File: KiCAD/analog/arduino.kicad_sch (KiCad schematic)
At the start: 49 parts, among them J12 Screw_Terminal_01x04, J13 Screw_Terminal_01x03, J14 Screw_Terminal_01x05, J17 Conn_Coaxial_Small, J18 Conn_Coaxial_Small, J19 Conn_Coaxial_Small, J20 Screw_Terminal_01x04, J21 Screw_Terminal_01x02, J22 Screw_Terminal_01x04, J23 Conn_Coaxial_Small, J24 Conn_Coaxial_Small, J6 Screw_Terminal_01x02, J7 Screw_Terminal_01x02, J8 Screw_Terminal_01x02, J9 Screw_Terminal_01x02, Q4 2N7000, Q5 2N7000, Q6 2N7000, Q7 2N7000, U1 MCP1700x-330xxTO, U17 Adafruit_PCF8575_Breakout, U18 CD14538B, U3 MCP4728

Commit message: KiCad revB: custom footprints, coax assignments, TO-92 widening, ENC_INT rewire
Second-pass footprint work: filled the remaining empty footprints
that couldn't be handled by the earlier stock-library scripts, added
custom footprints for parts KiCad's stock library doesn't cover, and
did a few schematic hygiene fixes surfaced during the deep-dive
reviews.

Custom footprints (new, xmitter.pretty/):
- SMA_Cinch_142-0701-201_Vertical_JackPCB - 50 Ohm SMA vertical
  through-hole jack for the analog board and bias board coax
  interconnects (I_CATHODE, GRID_CTL, GRID_BLOCK_CRASH, GRID_BIAS).
  Center pin 1.57 mm hole + 4 ground tabs on a 5.08 mm square
  pattern. All 4 ground tabs share pin number 2 (shield).
- CP_Radial_Kemet_ESK_D22.0mm_P10.00mm - Kemet ESK case Q4 radial
  electrolytic (22 mm dia, 10 mm pitch) for C72 = 4700 uF 50V.
- Fuse_Littelfuse_60R_L7.9mm_W3.1mm_P5.08mm - Littelfuse 60R Series
  radial polyfuse for F1 = 60R050XU (0.5 A hold). Body sized for the
  small-body variants (010X-090X); pitch 5.08 mm, drill 0.7 mm.
- C_Axial_Kemet_Aximax_C41X_L4.5mm_D2.6mm_P7.62mm_Horizontal - Kemet
  Aximax C410 axial C0G ceramic for the three 2 pF caps
  (C69/C70/C71) in the vfo_complete keyer chain. Horizontal mount,
  7.62 mm pitch.

New re-runnable script:
- tools/assign_coax_footprints.py - maps
  Connector:Conn_Coaxial_Small symbols to the new Cinch SMA
  footprint. Same "only fill empty, never overwrite" pattern as the
  existing assign_*_footprints.py scripts.

Script extension:
- tools/assign_cap_footprints.py - added value entries for 4700uF
  (Kemet ESK), 220nF (D6 disc), 2pF (Kemet Aximax C41X), and 100uF
  (Vishay 036 RSP). All four entries include the datasheet path and
  the specific case-size rationale.

Schematic edits (all boards):
- 12 coax connectors assigned to the new Cinch SMA footprint
  (analog J17-J19/J23-J24, bias J1/J2/J4/J6/J9/J10/J12) via the new
  assign_coax script.
- 5 caps in vfo_complete assigned via extended assign_cap_footprints
  (C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
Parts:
- F1: footprint (none) -> xmitter:Fuse_Littelfuse_60R_L7.9mm_W3.1mm_P5.08mm
- J17, J18, J19, J23, J24: footprint (none) -> xmitter:SMA_Cinch_142-0701-201_Vertical_JackPCB
- U1: footprint Package_TO_SOT_THT:TO-92_Inline -> Package_TO_SOT_THT:TO-92_Inline_Wide
- U3: footprint (none) -> xmitter:Adafruit_MCP4728_Breakout
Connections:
- net ENC_INT: now also C7.1, J9.2 (Pin_2), R6.2, R7.2; no longer R6.1
- net ENC_INT_CLEAN: now also R6.1; no longer C7.1, J9.2 (Pin_2), R6.2, R7.2
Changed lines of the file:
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@@
 		)
 	)
-	(global_label "ENC_INT_CLEAN"
+	(global_label "ENC_INT"
 		(shape input)
 		(at 46.99 66.04 90)
@@
 		)
 	)
-	(global_label "ENC_INT"
+	(global_label "ENC_INT_CLEAN"
 		(shape input)
 		(at 73.66 66.04 0)
@@
 			)
 		)
-		(property "Footprint" ""
+		(property "Footprint" "xmitter:Adafruit_MCP4728_Breakout"
 			(at 69.85 35.56 0)
 			(hide yes)
@@
 			)
 		)
-		(property "Footprint" ""
+		(property "Footprint" "xmitter:SMA_Cinch_142-0701-201_Vertical_JackPCB"
 			(at 121.92 119.38 0)
 			(hide yes)
@@
 			)
 		)
-		(property "Footprint" ""
+		(property "Footprint" "xmitter:SMA_Cinch_142-0701-201_Vertical_JackPCB"
 			(at 95.25 40.64 0)
 			(hide yes)
@@
 			)
 		)
-		(property "Footprint" ""
+		(property "Footprint" "xmitter:SMA_Cinch_142-0701-201_Vertical_JackPCB"
 			(at 78.74 157.48 0)
 			(hide yes)
@@
 			)
 		)
-		(property "Footprint" ""
+		(property "Footprint" "xmitter:SMA_Cinch_142-0701-201_Vertical_JackPCB"
 			(at 95.25 36.83 0)
 			(hide yes)
@@
 			)
 		)
-		(property "Footprint" ""
+		(property "Footprint" "xmitter:SMA_Cinch_142-0701-201_Vertical_JackPCB"
 			(at 118.11 138.43 0)
 			(hide yes)
@@
 			)
 		)
-		(property "Footprint" ""
+		(property "Footprint" "xmitter:Fuse_Littelfuse_60R_L7.9mm_W3.1mm_P5.08mm"
 			(at 104.14 99.06 0)
 			(hide yes)
@@
 			)
 		)
-		(property "Footprint" "Package_TO_SOT_THT:TO-92_Inline"
+		(property "Footprint" "Package_TO_SOT_THT:TO-92_Inline_Wide"
 			(at 173.99 25.4 0)
 			(hide yes)

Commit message: revB frozen state: MCP4922 swap + LDAC decouple + sheet rename + protoshield work
Captures the in-flight state of revB at the point where the project pivoted
to a full-SS output stage on a new branch (SS_Rev_C, cut from this commit).
revB is retained as a fallback if the SS PA plan on revC proves inadequate.

Included changes:
- Analog: MCP4921 (single DAC) replaced with MCP4922 (dual DAC). Channel
  assignment: DAC_A -> PA_OUTPUT_LEVEL (new global label, awaiting PA
  board), DAC_B -> Gate 2 (DGFET envelope keyer). Channels swapped from
  initial-design intent for layout convenience.
- Analog: DAC_LDAC_N decoupled from PCF8575 P5 (that global label renamed
  to PCF_P5_SPARE). Intent: route LDAC to Metro A4 for zero-latency
  simultaneous-DAC-update capability. Physical route to A4 NOT yet added
  -- DAC_LDAC_N label on dac.kicad_sch is dangling and will fail ERC.
- Analog: KiCad-driven used_designators bookkeeping (analog.kicad_pro).
- Sheet rename: KiCAD/analog/untitled.kicad_sch -> dac.kicad_sch. Root
  schematic Sheetfile reference updated.
- Protoshield: 537 lines of additions to protoshield.kicad_sch (user
  work). Not reviewed in this commit -- carried forward as-is.
- .gitignore: added tools/_*.py exclusion (local review-helper scripts).

**revB is NOT fab-ready in this state.** See memory
project_revB_pre_fab_check.md (outside repo) for the punch list. If the
SS PA plan ever reverses and someone revives revB, ALL open items must
be closed and a full pass through Documentation/pcb_fab_checklist.md
must be completed before any gerber submit.

Co-Authored-By: Claude Opus 4.7 <noreply@anthropic.com>
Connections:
- net GND: no longer J14.4 (Pin_4)
- net DAC_SHDN_N: now reaches U17.P6
- new net PCF_P5_SPARE: J14.4 (Pin_4)
- no-connect marks 23 -> 22
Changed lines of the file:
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@@
 	)
 	(no_connect
-		(at 175.26 81.28)
-	)
-	(no_connect
 		(at 175.26 68.58)
 	)
@@
 	)
 	(no_connect
-		(at 175.26 83.82)
+		(at 175.26 81.28)
 	)
 	(no_connect
@@
 		)
 	)
+	(global_label "PCF_P5_SPARE"
+		(shape input)
+		(at 30.48 110.49 0)
+		(fields_autoplaced yes)
+		(effects
+			(font
+				(size 1.27 1.27)
+			)
+			(justify left)
+		)
+		(property "Intersheetrefs" "${INTERSHEET_REFS}"
+			(at 45.0162 110.49 0)
+			(hide yes)
+			(show_name no)
+			(do_not_autoplace no)
+			(effects
+				(font
+					(size 1.27 1.27)
+				)
+				(justify left)
+			)
+		)
+	)
 	(global_label "GRID_CTL_B"
 		(shape output)
@@
 		)
 	)
+	(global_label "DAC_SHDN_N"
+		(shape output)
+		(at 175.26 83.82 180)
+		(fields_autoplaced yes)
+		(effects
+			(font
+				(size 1.27 1.27)
+			)
+			(justify right)
+		)
+		(property "Intersheetrefs" "${INTERSHEET_REFS}"
+			(at 160.24 83.82 0)
+			(hide yes)
+			(show_name no)
+			(do_not_autoplace no)
+			(effects
+				(font
+					(size 1.27 1.27)
+				)
+				(justify right)
+			)
+		)
+	)
 	(global_label "GRID_BLOCK_CRASH"
 		(shape input)
@@
 					(unit 1)
 				)
-			)
-		)
-	)
-	(symbol
-		(lib_id "power:GND")
-		(at 30.48 110.49 90)
-		(unit 1)
-		(body_style 1)
-		(exclude_from_sim no)
-		(in_bom yes)
-		(on_board yes)
-		(in_pos_files yes)
-		(dnp no)
-		(fields_autoplaced yes)
-		(property "Reference" "#PWR010"
-			(at 36.83 110.49 0)
-			(hide yes)
-			(show_name no)
-			(do_not_autoplace no)
-			(effects
-				(font
-					(size 1.27 1.27)
-				)
-			)
-		)
-		(property "Value" "GND"
-			(at 34.29 110.4899 90)
-			(show_name no)
-			(do_not_autoplace no)
-			(effects
-				(font
-					(size 1.27 1.27)
-				)
-				(justify right)
-			)
-		)
-		(property "Footprint" ""
-			(at 30.48 110.49 0)
-			(hide yes)
-			(show_name no)
-			(do_not_autoplace no)
-			(effects
-				(font
-					(size 1.27 1.27)
-				)
-			)
-		)
-		(property "Datasheet" ""
-			(at 30.48 110.49 0)
-			(hide yes)
-			(show_name no)
-			(do_not_autoplace no)
-			(effects
-				(font
-					(size 1.27 1.27)
-				)
-			)
-		)
-		(property "Description" "Power symbol creates a global label with name \"GND\" , ground"
-			(at 30.48 110.49 0)
-			(hide yes)
-			(show_name no)
-			(do_not_autoplace no)
-			(effects
-				(font
-					(size 1.27 1.27)
-				)
-			)
-		)
-		(pin "1"
-		)
-		(instances
-			(project "analog"
-				(path "/d3de40b8-856b-4fbd-829c-f45ffcd55742/2d83d0b5-86d4-4ced-ab68-6465e3dc2d72"
-					(reference "#PWR010")
-					(unit 1)
-				)

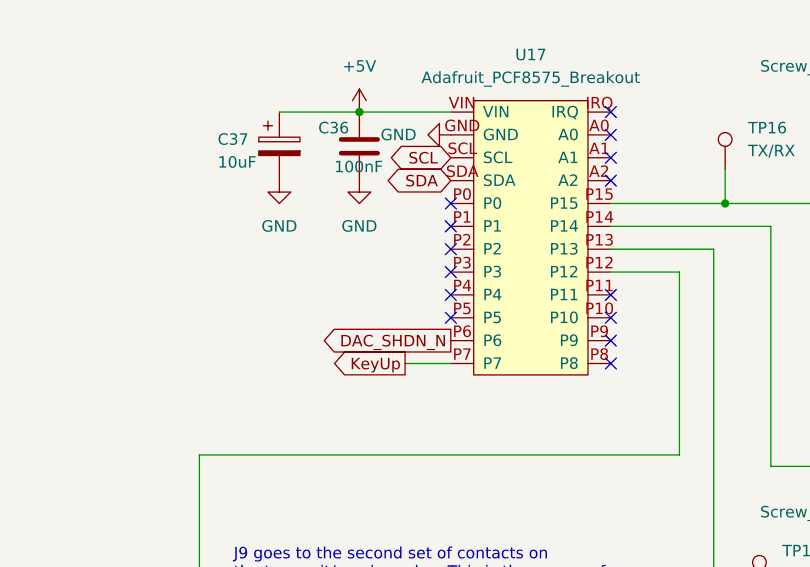
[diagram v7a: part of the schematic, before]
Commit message: KiCad revC: 4-band LPF bank populated + pad values + A_L units fix
Analog board revC: the LPF sheet is now fully populated with the
4-band relay-switched LPF bank architecture discussed in prior
sessions.  VFO sheet refactored to remove the old single-LPF stage.

LPF bank (lpf.kicad_sch):
  - 4 branches tied to a common input bus from U2 (LM7171 buffer).
    Common bus driven through C9 100nF; U2 non-inverting gain = 5.7.
  - Per-branch: 10 dB pi attenuator (100/68/100 ohm) -> 7-element
    Chebyshev CLCLCLC LPF (0.1 dB ripple, 50 ohm) -> 50 ohm RT
    terminator -> SPST relay (K1-K4) -> common output bus
    "Conditioned RF" -> R39 (0R) -> U10 input on VFO sheet.
  - Relay drive: 2N7000 low-side switcher (Q1/Q3/Q8/Q9) + 1N4148
    flyback diode (D7-D10) + screw terminal (J16/J25/J26/J27) per
    relay for coil wire termination.
  - LPF components: CF3-CF21 and L4-L17 populated with 20 m values
    (220 pF / 390 pF / 680 nH / 790 nH) on all four branches.
    Other-band values TBD per Documentation/lpf_component_values.md.
  - Pi pad resistors are now 100/68/100 (10 dB) rather than the
    initially-populated 62/240/62 (20 dB).  Reasoning: with permanent
    50 ohm termination at each LPF output and relay-based output
    switching, the pi pads are only providing impedance isolation at
    the common input bus, not inter-LPF signal isolation (which is
    handled by relay off-isolation of ~40 dB per open contact).
    10 dB is sufficient and recovers ~10 dB of noise margin.

VFO sheet (vfo_complete.kicad_sch):
  - Old inline LPF removed; VFO now feeds C10 -> U2 (on LPF sheet)
    via sheet-boundary net.
  - U10/U11/U12 LM7171 chain (post-LPF-bank amplifier + PP driver
    pair) retained.

Documentation/lpf_component_values.md (new):
  - Component values for all four bands (20/17/15/10 m).
  - 7-element Chebyshev CLCLCLC, 0.1 dB ripple, 50 ohm.
  - Per-band tables for T50-6 and T68-6 turn counts.
  - Notes on A_L unit convention (catalogs use uH/100T^2 not nH/N^2).

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
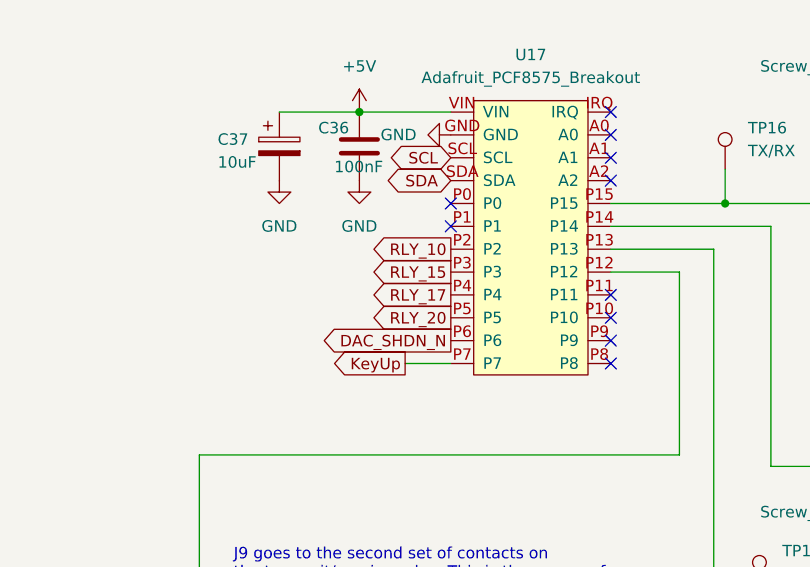
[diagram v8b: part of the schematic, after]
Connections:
- net RLY_10: now reaches U17.P2
- net RLY_15: now reaches U17.P3
- net RLY_17: now reaches U17.P4
- net RLY_20: now reaches U17.P5
- no-connect marks 22 -> 18
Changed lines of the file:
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@@
-	)
-	(no_connect
-		(at 175.26 73.66)
 	)
 	(no_connect
@@
 	)
 	(no_connect
-		(at 175.26 76.2)
-	)
-	(no_connect
 		(at 80.01 31.75)
 	)
@@
 	)
 	(no_connect
-		(at 175.26 81.28)
-	)
-	(no_connect
 		(at 167.64 142.24)
-	)
-	(no_connect
-		(at 175.26 78.74)
 	)
 	(no_connect
@@
 		)
 	)
+	(global_label "RLY_20"
+		(shape output)
+		(at 175.26 81.28 180)
+		(fields_autoplaced yes)
+		(effects
+			(font
+				(size 1.27 1.27)
+			)
+			(justify right)
+		)
+		(property "Intersheetrefs" "${INTERSHEET_REFS}"
+			(at 165.5015 81.28 0)
+			(hide yes)
+			(show_name no)
+			(do_not_autoplace no)
+			(effects
+				(font
+					(size 1.27 1.27)
+				)
+				(justify right)
+			)
+		)
+	)
 	(global_label "MBL600_A"
 		(shape output)
@@
 				)
 				(justify left)
+			)
+		)
+	)
+	(global_label "RLY_10"
+		(shape output)
+		(at 175.26 73.66 180)
+		(fields_autoplaced yes)
+		(effects
+			(font
+				(size 1.27 1.27)
+			)
+			(justify right)
+		)
+		(property "Intersheetrefs" "${INTERSHEET_REFS}"
+			(at 165.5015 73.66 0)
+			(hide yes)
+			(show_name no)
+			(do_not_autoplace no)
+			(effects
+				(font
+					(size 1.27 1.27)
+				)
+				(justify right)
 			)
 		)
@@
 		)
 	)
+	(global_label "RLY_17"
+		(shape output)
+		(at 175.26 78.74 180)
+		(fields_autoplaced yes)
+		(effects
+			(font
+				(size 1.27 1.27)
+			)
+			(justify right)
+		)
+		(property "Intersheetrefs" "${INTERSHEET_REFS}"
+			(at 165.5015 78.74 0)
+			(hide yes)
+			(show_name no)
+			(do_not_autoplace no)
+			(effects
+				(font
+					(size 1.27 1.27)
+				)
+				(justify right)
+			)
+		)
+	)
 	(global_label "GRID_CTL_A"
 		(shape output)
@@
 			)
 		)
+	)
+	(global_label "RLY_15"
+		(shape output)
+		(at 175.26 76.2 180)
+		(fields_autoplaced yes)
+		(effects
+			(font
+				(size 1.27 1.27)
+			)
+			(justify right)
+		)
+		(property "Intersheetrefs" "${INTERSHEET_REFS}"
+			(at 165.5015 76.2 0)
+			(hide yes)
+			(show_name no)
+			(do_not_autoplace no)
+			(effects
+				(font
+					(size 1.27 1.27)
+				)
+				(justify right)
+			)
+		)
